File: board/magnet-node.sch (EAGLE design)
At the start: 37 parts, among them IC1 HTU21D, X1 SMA-142-0701-801/806, X2 SMA-142-0711-821/826

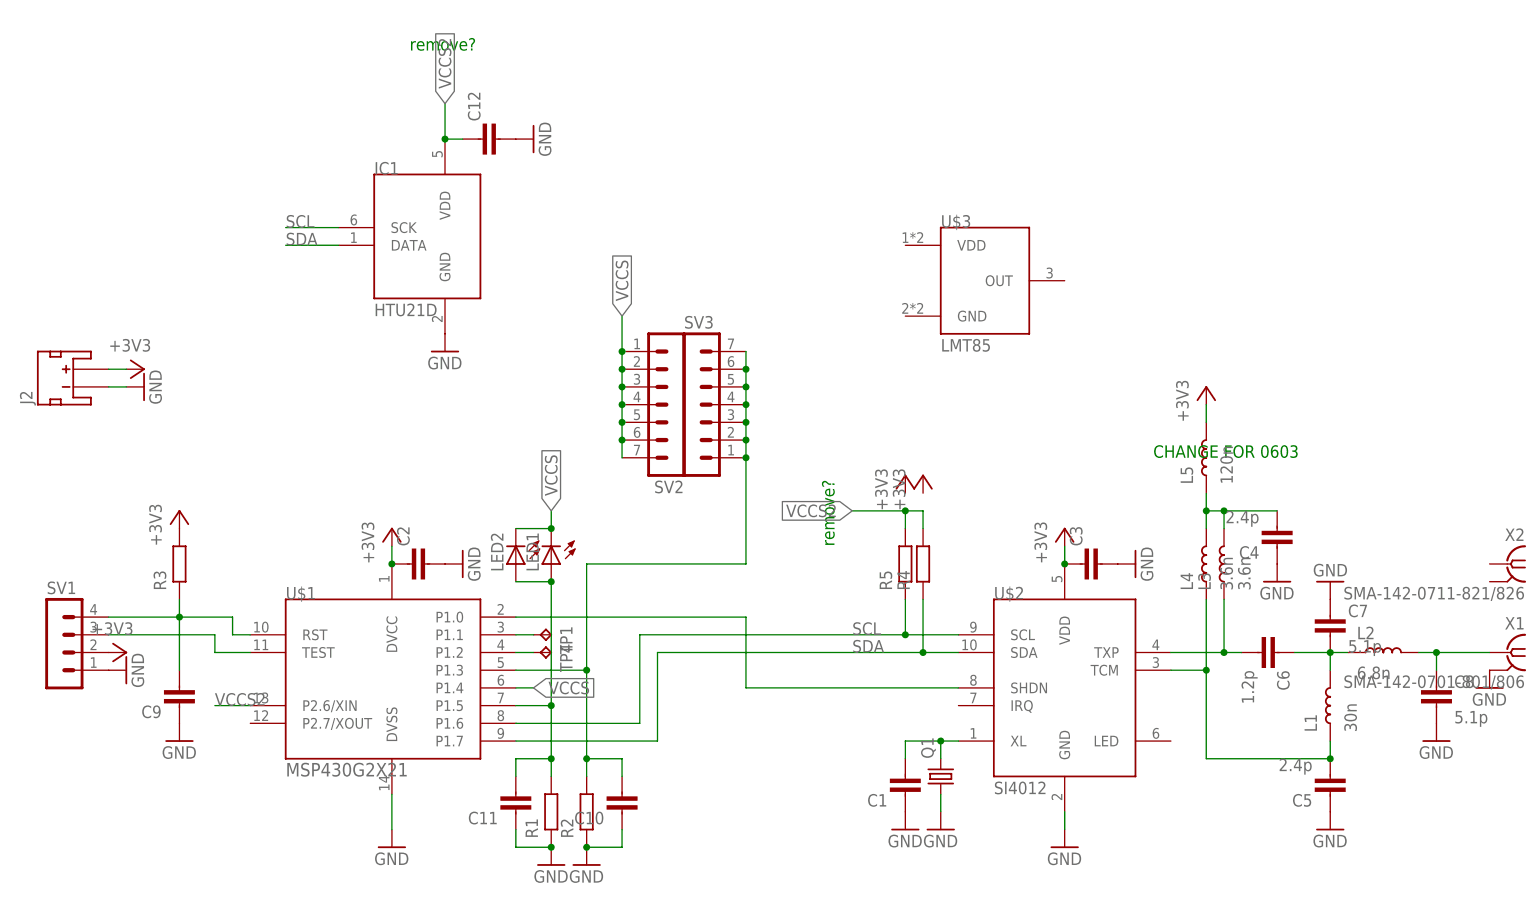
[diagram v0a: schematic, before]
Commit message: removed power control from dht
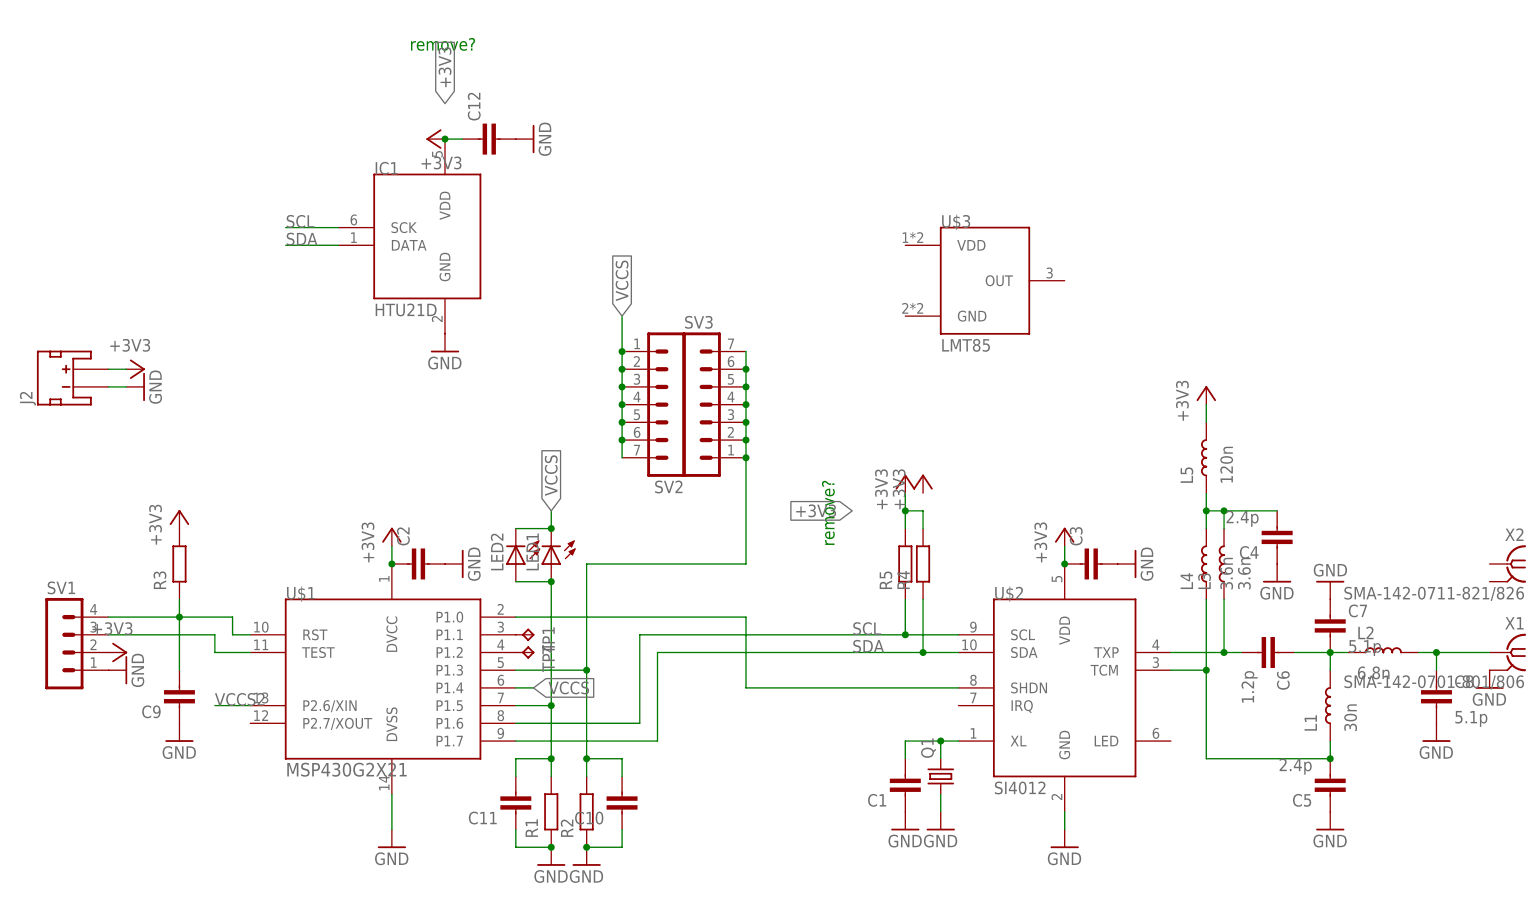
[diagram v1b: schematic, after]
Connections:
- net +3V3: now also C12.1, IC1.VDD, R4.P$2, R5.P$2
- net VCCS2: no longer C12.1, IC1.VDD, R4.P$2, R5.P$2
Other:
- note removed: "CHANGE FOR 0603"
- moved on the sheet: TP1, TP4
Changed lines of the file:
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@@
 <part name="TP4" library="testpad" deviceset="TP" device="TP14SQ"/>
 <part name="TP1" library="testpad" deviceset="TP" device="TP14SQ"/>
+<part name="+3V6" library="supply1" deviceset="+3V3" device=""/>
 </parts>
 <sheets>
@@
 <text x="48.26" y="132.08" size="1.778" layer="91">remove?</text>
 <text x="109.22" y="60.96" size="1.778" layer="91" rot="R90">remove?</text>
-<text x="154.94" y="73.66" size="1.778" layer="91">CHANGE FOR 0603</text>
 </plain>
 <instances>
@@
 <instance part="L4" gate="G$1" x="162.56" y="58.42" rot="R90"/>
 <instance part="L5" gate="G$1" x="162.56" y="73.66" rot="R90"/>
-<instance part="TP4" gate="G$1" x="68.58" y="45.72" rot="R270"/>
-<instance part="TP1" gate="G$1" x="68.58" y="48.26" rot="R270"/>
+<instance part="TP4" gate="G$1" x="66.04" y="45.72" rot="R270"/>
+<instance part="TP1" gate="G$1" x="66.04" y="48.26" rot="R270"/>
+<instance part="+3V6" gate="G$1" x="50.8" y="119.38" rot="R90"/>
 </instances>
 <busses>
@@
 <pinref part="+3V5" gate="G$1" pin="+3V3"/>
 <wire x1="162.56" y1="78.74" x2="162.56" y2="81.28" width="0.1524" layer="91"/>
+</segment>
+<segment>
+<pinref part="R4" gate="G$1" pin="P$2"/>
+<wire x1="121.92" y1="63.5" x2="121.92" y2="66.04" width="0.1524" layer="91"/>
+<wire x1="121.92" y1="66.04" x2="119.38" y2="66.04" width="0.1524" layer="91"/>
+<pinref part="R5" gate="G$1" pin="P$2"/>
+<wire x1="119.38" y1="63.5" x2="119.38" y2="66.04" width="0.1524" layer="91"/>
+<label x="111.76" y="66.04" size="1.778" layer="95" rot="R180" xref="yes"/>
+<pinref part="+3V9" gate="G$1" pin="+3V3"/>
+<wire x1="119.38" y1="68.58" x2="119.38" y2="66.04" width="0.1524" layer="91"/>
+<junction x="119.38" y="66.04"/>
+</segment>
+<segment>
+<pinref part="C12" gate="G$1" pin="1"/>
+<wire x1="55.88" y1="119.38" x2="53.34" y2="119.38" width="0.1524" layer="91"/>
+<label x="53.34" y="124.46" size="1.778" layer="95" rot="R90" xref="yes"/>
+<pinref part="IC1" gate="G$1" pin="VDD"/>
+<pinref part="+3V6" gate="G$1" pin="+3V3"/>
+<junction x="53.34" y="119.38"/>
 </segment>
 </net>
@@
 <segment>
 <pinref part="U$1" gate="G$1" pin="P1.1"/>
-<wire x1="63.5" y1="48.26" x2="66.04" y2="48.26" width="0.1524" layer="91"/>
 <pinref part="TP1" gate="G$1" pin="TP"/>
 </segment>
@@
 <segment>
 <pinref part="U$1" gate="G$1" pin="P1.2"/>
-<wire x1="66.04" y1="45.72" x2="63.5" y2="45.72" width="0.1524" layer="91"/>
 <pinref part="TP4" gate="G$1" pin="TP"/>
 </segment>
@@
 <label x="20.32" y="38.1" size="1.778" layer="95"/>
 </segment>
-<segment>
-<pinref part="C12" gate="G$1" pin="1"/>
-<wire x1="55.88" y1="119.38" x2="53.34" y2="119.38" width="0.1524" layer="91"/>
-<wire x1="53.34" y1="119.38" x2="53.34" y2="124.46" width="0.1524" layer="91"/>
-<label x="53.34" y="124.46" size="1.778" layer="95" rot="R90" xref="yes"/>
-<pinref part="IC1" gate="G$1" pin="VDD"/>
-<junction x="53.34" y="119.38"/>
-</segment>
-<segment>
-<pinref part="R4" gate="G$1" pin="P$2"/>
-<wire x1="121.92" y1="63.5" x2="121.92" y2="66.04" width="0.1524" layer="91"/>
-<wire x1="121.92" y1="66.04" x2="119.38" y2="66.04" width="0.1524" layer="91"/>
-<pinref part="R5" gate="G$1" pin="P$2"/>
-<wire x1="119.38" y1="66.04" x2="111.76" y2="66.04" width="0.1524" layer="91"/>
-<wire x1="119.38" y1="63.5" x2="119.38" y2="66.04" width="0.1524" layer="91"/>
-<label x="111.76" y="66.04" size="1.778" layer="95" rot="R180" xref="yes"/>
-<junction x="119.38" y="66.04"/>
-</segment>
-</net>
+</net>

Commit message: almost ready to do
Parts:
- removed SV1: (no value), Mine:MA04-1E
- removed TP1, TP4: TPTP14SQ, testpad:TPTP14SQ
- removed U$3: LMT85, Mine:LMT85
- removed X1: SMA-142-0701-801/806, con-coax:SMA-142-0701-801/806
- removed X2: SMA-142-0711-821/826, con-coax:SMA-142-0711-821/826
- added IC2: HTU21D, Mine:HTU21D
- C1, C2, C3: value (none) -> 100n
- C10: value (none) -> 47n
- C11: value (none) -> 2.4p
- C12: value (none) -> 14p
- C4: value 2.4p -> (none)
- C5: value 2.4p -> 5.1p
- C6: value 1.2p -> 5.1p
- C7: value 5.1p -> 1u
- C8: value 5.1p -> 2.4p
- C9: value (none) -> 1.2p
- IC1: value HTU21D -> MSP430G2X21; device Mine:HTU21D -> Mine:MSP430G2X21
- L1: value 30n -> 120n; device passives-7351:INDUCTOR0402-N -> passives-7351:INDUCTOR0603-N
- L2: value 6.8n -> 3.6n
- L3: value 3.6n -> 6.8n
- L4: value 3.6n -> 30n
- L5: value 120n -> 3.6n; device passives-7351:INDUCTOR0603-N -> passives-7351:INDUCTOR0402-N
- R1: value (none) -> 47k
- R2: value (none) -> 1M
- R3: value (none) -> 22k
- R4, R5: value (none) -> 4k7
- SV3: device Mine:MA07-1S -> Mine:MA04-1E
- U$1: value MSP430G2X21 -> MA06-1; device Mine:MSP430G2X21 -> Mine:MA06-1
- renumbered J2 to J1, U$2 to IC3
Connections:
- removed net N$11: TP1.TP, U$1.P1.1
- removed net N$14: TP4.TP, U$1.P1.2
- new net IO1: IC1.P1.1, SV2.6
- new net IO2: IC1.P1.2, SV2.5
- net +3V3: now also C4.1, C7.1, IC1.DVCC, IC2.VDD, L1.P$2, SV3.2; no longer C12.1, C2.1, IC1.VDD, L5.P$2, SV1.2, U$1.DVCC
- net GND: now also C12.1, C2.1, C4.2, C6.2, C7.2, C8.1, IC1.DVSS, IC2.GND, SV2.7, SV3.1; no longer C12.2, C2.2, C4.1, C7.1, C8.2, C9.1, IC1.GND, SV1.1, U$1.DVSS, X1.2
- net N$1: now also IC1.P1.0; no longer U$1.P1.0
- net N$10: now also C6.1, L3.P$2; no longer C8.1, L2.P$2, X1.1
- net N$12: now also C1.2, IC1.P1.3, R1.P$2, U$1.1, U$1.2, U$1.3, U$1.4, U$1.5, U$1.6; no longer C10.2, R2.P$2, SV3.1, SV3.2, SV3.3, SV3.4, SV3.5, SV3.6, SV3.7, U$1.P1.3
- net N$13: now also C2.2, IC1.P1.5, R2.P$2; no longer C11.2, R1.P$2, U$1.P1.5
- net N$15: now also C10.2, IC1.RST, SV3.4; no longer C9.2, SV1.4, U$1.RST
- net N$2: now also IC1.TEST, SV3.3; no longer SV1.3, U$1.TEST
- net N$4: now also C8.2, L1.P$1, L2.P$2, L5.P$2; no longer C4.2, L3.P$2, L4.P$2, L5.P$1
- net N$5: now also C12.2; no longer C1.2
- net N$7: now also C5.2, C9.1, L3.P$1, L4.P$2; no longer C6.1, C7.2, L1.P$2, L2.P$1
- net N$8: now also C11.2, L5.P$1; no longer C5.2, L1.P$1
- net N$9: now also C9.2, L2.P$1; no longer C6.2, L3.P$1
- net SCL: now also IC1.P1.6, IC2.SCK; no longer IC1.SCK, U$1.P1.6
- net SDA: now also IC1.P1.7, IC2.DATA; no longer IC1.DATA, U$1.P1.7
- net VCCS: now also IC1.P1.4; no longer SV2.5, SV2.6, SV2.7, U$1.P1.4
- net VCCS2: now also IC1.P2.6/XIN; no longer U$1.P2.6/XIN
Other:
- moved on the sheet: C1, C10, C11, C12, C2, C3, C4, C5, C6, C7, C8, C9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
